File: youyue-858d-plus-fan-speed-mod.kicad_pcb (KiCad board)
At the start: 2 copper layers, 17 x 31 mm, 20 parts, among them P1 CONN_01X01, P2 CONN_01X01, P3 CONN_01X01, P4 CONN_01X01, U1 LM2904

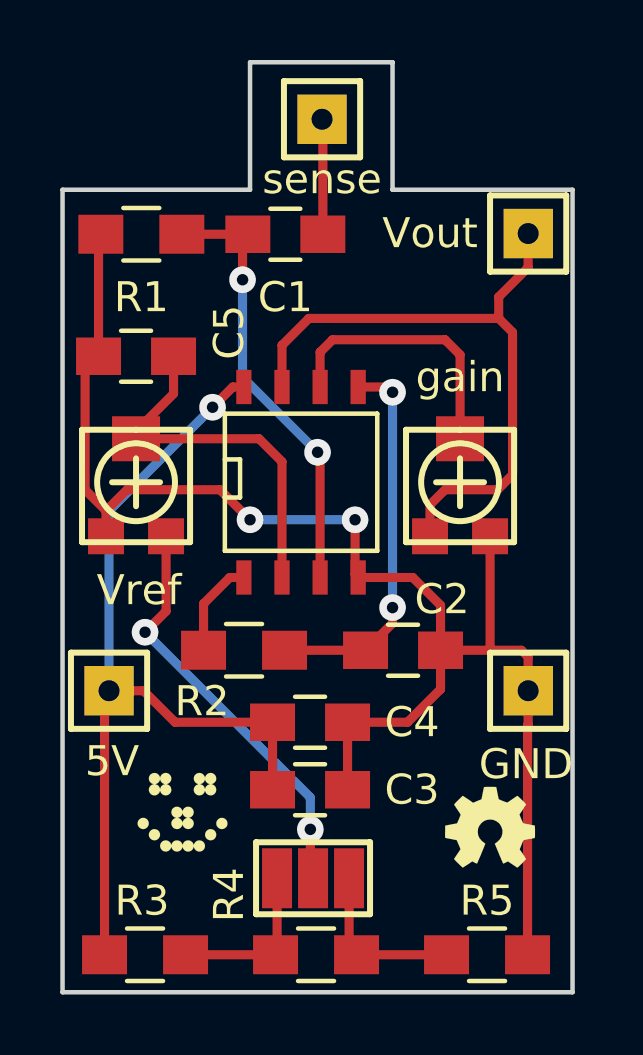
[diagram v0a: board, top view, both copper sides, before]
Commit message: Moved sense-pin to free spot.
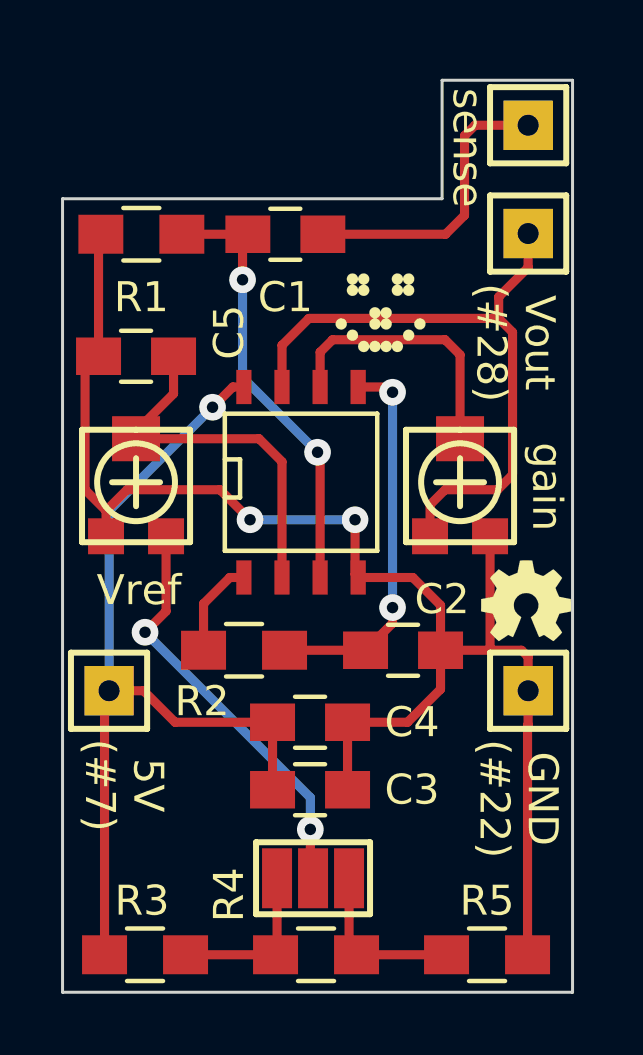
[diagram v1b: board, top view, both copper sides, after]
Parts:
- moved G*** 17.9 mm to (186.8, 31.9)
- moved G*** 7.64 mm to (191.7, 41.5)
- moved P1 6.87 mm to (191.8, 25.6)
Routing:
- net /I_BLDC: track 3.84 -> 9.94 mm
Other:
- board size 17 x 31 mm -> 17 x 30.4 mm
- board text added: "5V (#7)"
- board text added: "GND (#22)"
- board text added: "V0.10.b"
- board text added: "Vout (#28)"
- board text removed: "5V"
- board text removed: "GND"
- board text removed: "V0.10.a"
- board text removed: "Vout"
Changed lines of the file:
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@@
 (kicad_pcb (version 4) (host pcbnew "(2015-10-08 BZR 6256, Git 7d5cb75)-product")
   (general
-    (links 0)
+    (links 29)
     (no_connects 0)
-    (area 172.460267 21.4536 197.109734 56.5314)
+    (area 172.460267 21.6536 197.109734 56.5314)
     (thickness 1.6)
-    (drawings 16)
-    (tracks 100)
+    (drawings 14)
+    (tracks 104)
     (zones 0)
     (modules 20)
@@
     (title "Youyue 858D+ FAN-speed mod")
     (date 2015-10-09)
-    (rev 0.10)
+    (rev 0.10.b)
     (company "2015 - blog.spitzenpfeil.org")
   )
@@
     (trace_min 0.2032)
     (segment_width 0.2)
-    (edge_width 0.15)
+    (edge_width 0.1)
     (via_size 0.889)
     (via_drill 0.381)
@@
   )
   (module SIL-Headers:SIL-1 (layer F.Cu)
-    (at 184.9 25.4)
+    (at 191.77 25.6)
     (tags "CONN DEV")
     (fp_text reference P1 (at 0 -2.54) (layer F.SilkS) hide
@@
   )
   (module led-smile:LED_smile_silkscreen_3mm (layer F.Cu)
-    (at 180.25 48.5)
+    (at 186.85 31.85)
     (fp_text reference G*** (at 0 1.7272) (layer F.SilkS) hide
       (effects (font (size 0.0381 0.0381) (thickness 0.00762)))
@@
   )
   (module oshw-logo:OSHW-logo_silkscreen_3mm (layer F.Cu)
-    (at 190.5 49)
+    (at 191.7 41.45)
     (fp_text reference G*** (at 0 1.59004) (layer F.SilkS) hide
       (effects (font (size 0.13462 0.13462) (thickness 0.0254)))
@@
       (xy -0.90932 1.3462)) (layer F.SilkS) (width 0.00254))
   )
-  (gr_text V0.10.a (at 192 36.5 90) (layer B.SilkS)
+  (gr_line (start 188.9 24.1) (end 193.25 24.1) (layer Edge.Cuts) (width 0.1))
+  (gr_line (start 188.9 28.05) (end 188.9 24.1) (layer Edge.Cuts) (width 0.1))
+  (gr_text V0.10.b (at 192 36.5 90) (layer B.SilkS)
     (effects (font (size 1 1) (thickness 0.15)) (justify mirror))
   )
@@
     (effects (font (size 1 1) (thickness 0.15)) (justify mirror))
   )
-  (gr_line (start 193.25 54.5) (end 176.25 54.5) (layer Edge.Cuts) (width 0.15))
-  (gr_line (start 193.25 27.75) (end 193.25 54.5) (layer Edge.Cuts) (width 0.15))
-  (gr_line (start 187.25 27.75) (end 193.25 27.75) (layer Edge.Cuts) (width 0.15))
-  (gr_line (start 187.25 23.5) (end 187.25 27.75) (layer Edge.Cuts) (width 0.15))
-  (gr_line (start 182.5 23.5) (end 187.25 23.5) (layer Edge.Cuts) (width 0.15))
-  (gr_line (start 182.5 27.75) (end 182.5 23.5) (layer Edge.Cuts) (width 0.15))
-  (gr_line (start 176.25 27.75) (end 182.5 27.75) (layer Edge.Cuts) (width 0.15))
-  (gr_line (start 176.25 54.5) (end 176.25 27.75) (layer Edge.Cuts) (width 0.15))
+  (gr_line (start 193.25 54.5) (end 176.25 54.5) (layer Edge.Cuts) (width 0.1))
+  (gr_line (start 193.25 24.1) (end 193.25 54.5) (layer Edge.Cuts) (width 0.1))
+  (gr_line (start 176.25 28.05) (end 188.9 28.05) (layer Edge.Cuts) (width 0.1))
+  (gr_line (start 176.25 54.5) (end 176.25 28.05) (layer Edge.Cuts) (width 0.1))
   (gr_text Vref (at 178.8 41.1) (layer F.SilkS)
     (effects (font (size 1 1) (thickness 0.15)))
   )
-  (gr_text gain (at 189.5 34) (layer F.SilkS)
+  (gr_text gain (at 192.4 37.65 270) (layer F.SilkS)
     (effects (font (size 1 1) (thickness 0.15)))
   )
-  (gr_text Vout (at 188.5 29.2) (layer F.SilkS)
+  (gr_text "Vout\n(#28)" (at 191.35 32.85 270) (layer F.SilkS)
     (effects (font (size 1 1) (thickness 0.15)))
   )
-  (gr_text GND (at 191.7 46.9) (layer F.SilkS)
+  (gr_text "GND\n(#22)" (at 191.45 48.05 270) (layer F.SilkS)
     (effects (font (size 1 1) (thickness 0.15)))
   )
-  (gr_text 5V (at 177.9 46.8) (layer F.SilkS)
+  (gr_text "5V\n(#7)" (at 178.3 47.6 270) (layer F.SilkS)
     (effects (font (size 1 1) (thickness 0.15)))
   )
-  (gr_text sense (at 184.9 27.4) (layer F.SilkS)
+  (gr_text sense (at 189.75 26.35 270) (layer F.SilkS)
     (effects (font (size 1 1) (thickness 0.15)))
   )
-  (segment (start 184.926174 29.233456) (end 184.926174 25.426174) (width 0.3048) (layer F.Cu) (net 1) (status 30))
-  (segment (start 184.926174 25.426174) (end 184.9 25.4) (width 0.3048) (layer F.Cu) (net 1) (status 30))
+  (segment (start 189.65 28.6) (end 189.016544 29.233456) (width 0.3048) (layer F.Cu) (net 1))
+  (segment (start 189.016544 29.233456) (end 184.926174 29.233456) (width 0.3048) (layer F.Cu) (net 1))
+  (segment (start 189.65 25.95) (end 189.65 28.6) (width 0.3048) (layer F.Cu) (net 1))
+  (segment (start 190 25.6) (end 189.65 25.95) (width 0.3048) (layer F.Cu) (net 1))
+  (segment (start 191.77 25.6) (end 190 25.6) (width 0.3048) (layer F.Cu) (net 1))
+  (segment (start 191.776174 25.626174) (end 191.75 25.6) (width 0.3048) (layer F.Cu) (net 1) (status 30))
   (segment (start 182.25 30.75) (end 182.25 29.40963) (width 0.3048) (layer F.Cu) (net 2) (status 20))
   (segment (start 182.25 29.40963) (end 182.426174 29.233456) (width 0.3048) (layer F.Cu) (net 2) (status 30))

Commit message: Added indicator LED for easy(er) comparator adjustment (no DSO).
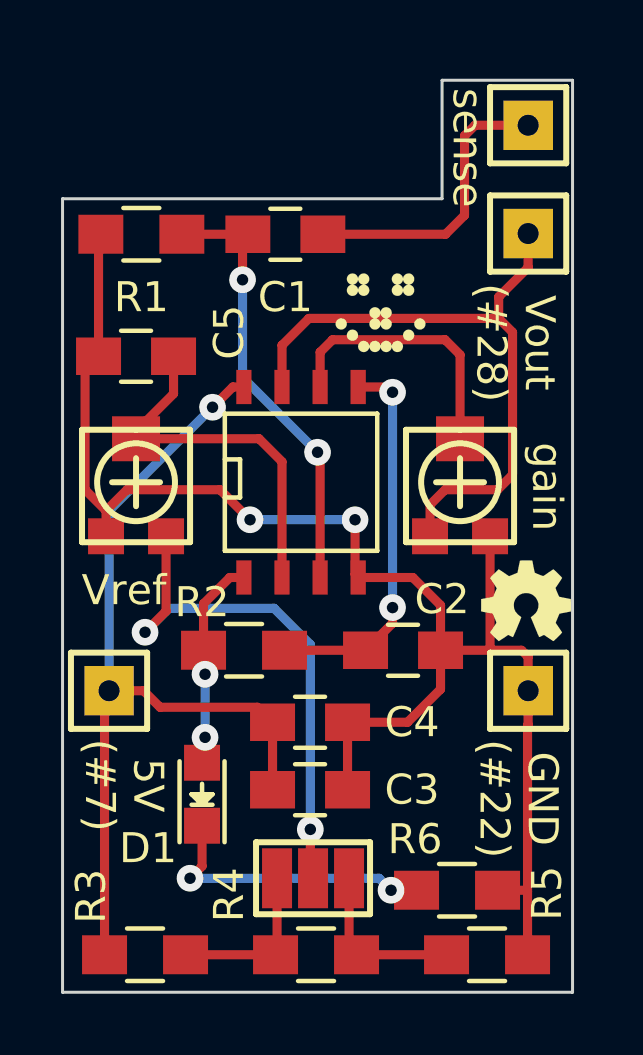
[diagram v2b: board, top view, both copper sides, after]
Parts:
- added D1: LED, LEDs:LED-0805, F.Cu at (180.9, 47.9)
- added R6: 1k, Resistors_SMD:R_0805_HandSoldering, F.Cu at (189.4, 51.1)
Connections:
- net Net-(R2-Pad2) renamed /comp_adj
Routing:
- net Net-(D1-Pad1): track 0.00 -> 9.63 mm, vias 0 -> 2
- net /comp_adj: track 3.26 -> 7.07 mm, vias 0 -> 2
- net Net-(JP1-Pad2): track 14.0 -> 17.7 mm
- net GND: track 50.1 -> 51.1 mm
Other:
- board text added: "V0.11.a"
- board text removed: "V0.10.b"

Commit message: Fixed 'C2' in schematic: falsely marked as electrolytic.
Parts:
- C2: value 1µ -> 1µF
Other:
- board text added: "V0.12.a"
- board text removed: "V0.11.a"
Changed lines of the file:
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@@
-(kicad_pcb (version 4) (host pcbnew "(2015-10-21 BZR 6273, Git ad10218)-product")
+(kicad_pcb (version 4) (host pcbnew "(2015-12-01 BZR 6337, Git 6f5a49b)-product")
   (general
     (links 32)
@@
   (title_block
     (title "Youyue 858D+ FAN-speed mod")
-    (date 2015-10-24)
-    (rev 0.11.a)
+    (date 2015-12-03)
+    (rev 0.12.a)
     (company "2015 - blog.spitzenpfeil.org")
   )
@@
       (effects (font (size 1 1) (thickness 0.15)))
     )
-    (fp_text value 1µ (at 0 2.1) (layer F.Fab) hide
+    (fp_text value 1µF (at 0 2.1) (layer F.Fab) hide
       (effects (font (size 1 1) (thickness 0.15)))
     )
@@
   (gr_line (start 188.9 24.1) (end 193.25 24.1) (layer Edge.Cuts) (width 0.1))
   (gr_line (start 188.9 28.05) (end 188.9 24.1) (layer Edge.Cuts) (width 0.1))
-  (gr_text V0.11.a (at 192 36.5 90) (layer B.SilkS)
+  (gr_text V0.12.a (at 192 36.5 90) (layer B.SilkS)
     (effects (font (size 1 1) (thickness 0.15)) (justify mirror))
   )
